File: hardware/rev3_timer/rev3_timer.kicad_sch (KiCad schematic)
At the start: 44 parts, among them J1 Conn_01x06, J2 Conn_02x03_Odd_Even, J3 Conn_01x06, J4 Conn_01x02, SW1 SW_Push, SW2 SW_Push, SW3 SW_Push, SW4 SW_Push, U1 ATmega168-20P, U15 LM7805_TO220, U16 SN76489, U17 LM380N

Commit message: working on placement
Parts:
- added Z1: BOM_Item, symbol my_misc:BOM_Item
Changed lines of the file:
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@@
     (pin "1")
+  )
+  (symbol (lib_id "my_misc:BOM_Item") (at 248.92 129.54 0) (unit 1)
+    (in_bom yes) (on_board no) (fields_autoplaced)
+    (property "Reference" "Z1" (id 0) (at 257.81 130.8099 0)
+      (effects (font (size 1.27 1.27)) (justify left))
+    )
+    (property "Value" "BOM_Item" (id 1) (at 247.65 124.46 0)
+      (effects (font (size 1.27 1.27)) hide)
+    )
+    (property "Footprint" "" (id 2) (at 248.92 129.54 0)
+      (effects (font (size 1.27 1.27)) hide)
+    )
+    (property "Datasheet" "" (id 3) (at 248.92 129.54 0)
+      (effects (font (size 1.27 1.27)) hide)
+    )
+    (property "Vendor" "Vendor" (id 4) (at 257.81 133.3499 0)
+      (effects (font (size 1.27 1.27)) (justify left))
+    )
+    (property "CatNo" "(50) pcs ED90587-ND" (id 5) (at 257.81 135.8899 0)
+      (effects (font (size 1.27 1.27)) (justify left))
+    )
   )
   (symbol (lib_id "power:GND") (at 91.44 69.85 0) (mirror y) (unit 1)
@@
       (reference "C16") (unit 1) (value "220uF 25V") (footprint "Capacitor_THT:CP_Radial_D6.3mm_P2.50mm")
     )
+    (path "/9ab3b900-a094-457f-a2cb-e9fc0e76c390/398d97b2-4294-441d-8447-91ccf3db6f16"
+      (reference "C17") (unit 1) (value "0.1uF") (footprint "Capacitor_THT:C_Disc_D3.0mm_W1.6mm_P2.50mm")
+    )
     (path "/85142539-10c2-4f17-b1f7-d3e634808e0d"
       (reference "D1") (unit 1) (value "1N4007") (footprint "Diode_THT:D_DO-41_SOD81_P10.16mm_Horizontal")
@@
       (reference "U19") (unit 1) (value "SN75468") (footprint "Package_DIP:DIP-16_W7.62mm_Socket")
     )
-  )
+    (path "/20f5d1d2-5742-4763-bb11-c89799e997ac"
+      (reference "Z1") (unit 1) (value "BOM_Item") (footprint "")
+    )
+  )

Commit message: working on two-board design
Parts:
- added H1, H2, H3, H4, H5, H6, H7, H8: MountingHole, MountingHole:MountingHole_4.3mm_M4_Pad, symbol Mechanical:MountingHole
- added J? (x2): Conn_01x10, symbol Connector_Generic:Conn_01x10
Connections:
- net display/NE_CTL: now also J?.4 (Pin_4); no longer U1.5 (PD3)
- net display/SR_CLK: now also J?.2 (Pin_2); no longer U1.15 (PB1)
- net display/SR_DATA: now also J?.3 (Pin_3); no longer U1.16 (PB2)
- net display/SR_nRST: now also J?.1 (Pin_1); no longer U1.14 (PB0)
- new net: J?.1 (Pin_1), U1.14 (PB0)
- new net: J?.2 (Pin_2), U1.15 (PB1)
- new net: J?.3 (Pin_3), U1.16 (PB2)
- new net: J?.4 (Pin_4), U1.5 (PD3)

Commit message: playing with placement
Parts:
- added J7, J8: Conn_01x04, Connector_PinHeader_2.54mm:PinHeader_1x04_P2.54mm_Vertical, symbol Connector_Generic:Conn_01x04
- J5, J6: renamed from J?; footprint (none) -> Connector_PinHeader_2.54mm:PinHeader_2x05_P2.54mm_Vertical
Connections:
- net 180V: now also J7.1 (Pin_1), J8.1 (Pin_1)
- net GND: now also J5.10 (Pin_10), J5.9 (Pin_9), J6.10 (Pin_10), J6.9 (Pin_9), J7.4 (Pin_4), J8.4 (Pin_4)
- net VCC: now also J5.7 (Pin_7), J5.8 (Pin_8), J6.7 (Pin_7), J6.8 (Pin_8)

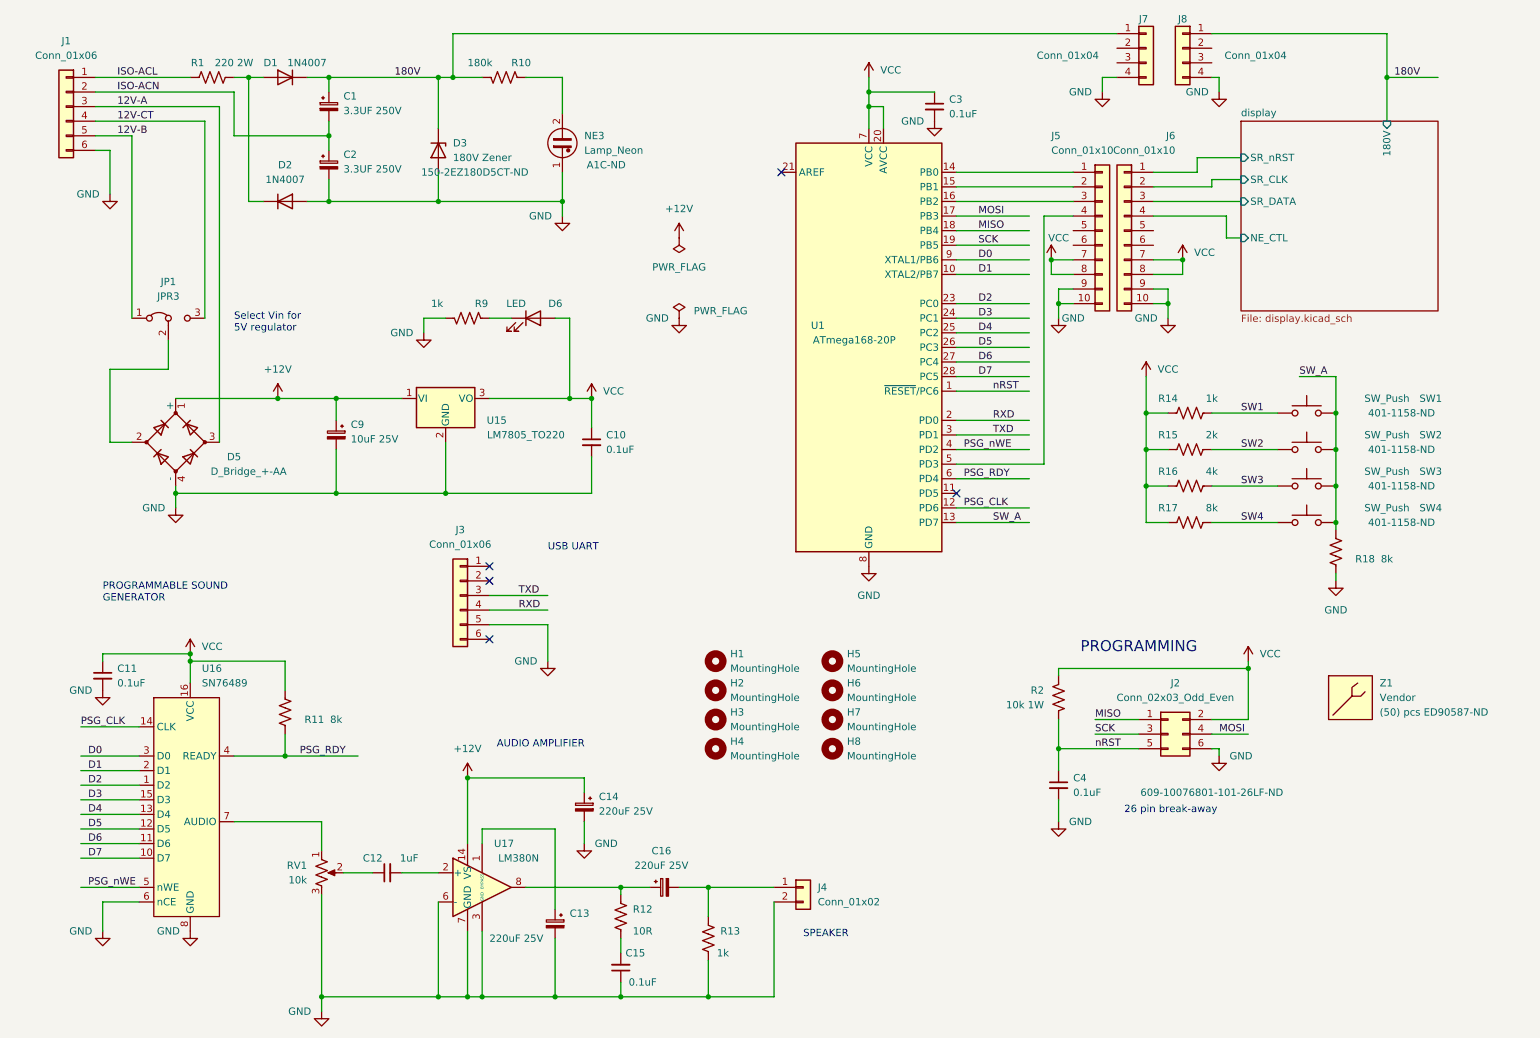
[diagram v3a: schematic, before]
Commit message: add RTC, rearrange placement
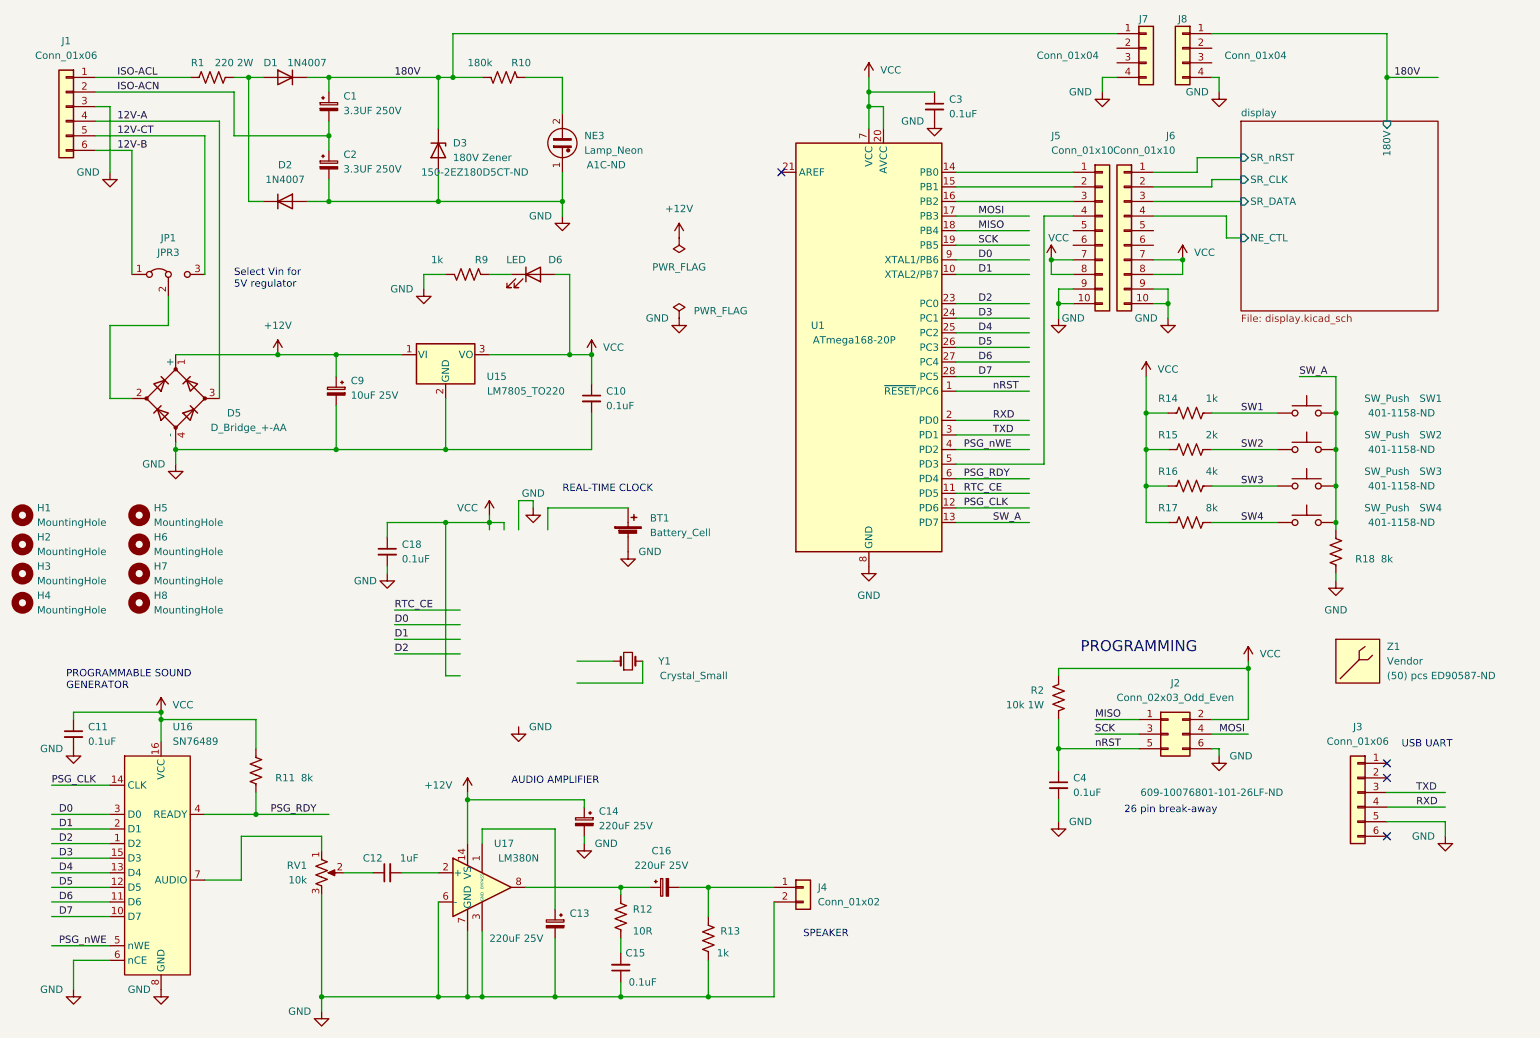
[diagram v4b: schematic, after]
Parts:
- added BT1: Battery_Cell, symbol Device:Battery_Cell
- added C18: 0.1uF, Capacitor_THT:C_Disc_D3.0mm_W1.6mm_P2.50mm, symbol Device:C_Small
- added Y1: Crystal_Small, Crystal:Crystal_C26-LF_D2.1mm_L6.5mm_Horizontal, symbol Device:Crystal_Small
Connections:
- net 12V-A: now also J1.4 (Pin_4); no longer J1.3 (Pin_3)
- net 12V-B: now also J1.6 (Pin_6); no longer J1.5 (Pin_5)
- net 12V-CT: now also J1.5 (Pin_5); no longer J1.4 (Pin_4)
- net GND: now also J1.3 (Pin_3), BT1.2 (-), C18.2; no longer J1.6 (Pin_6)
- net VCC: now also C18.1
- net RTC_CE: now reaches U1.11 (PD5)
- no-connect marks 5 -> 4
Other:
- note added: "REAL-TIME CLOCK"
- moved on the sheet: C10, C11, C14, C9, D5, D6, H1, H2, H3, H4, H5, H6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
